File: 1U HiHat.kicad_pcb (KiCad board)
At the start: 2 copper layers, 55.9 x 58.4 mm, 129 parts, among them J1 OH_TRIG, J10 MB, J2 ACCENT, J3 CH_TRIG, J4 OH_OUT, J5 CH_OUT, J6 CB, J7 MB, J8 PWR, J9 CB, P1 2M, P2 A100k, P3 A100k, Q1 BC856, Q10 BC846, Q11 BC846, Q12 BC846, Q13 BC846, Q14 BC846, Q2 BC856, Q3 BC846, Q4 BC846, Q5 BC846, Q6 BC846, Q7 BC846, Q8 BC846, Q9 BC846, U1 TL072, U2 TL072, U3 4584, U4 78L05

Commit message: Complete redesign started
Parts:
- removed REF**: Perforacija, MojaBiblioteka:Perforacija
- C31: value 220n -> 2.2u
- D1, D2: value 1n914 -> 1N914; footprint Diodes_SMD:D_SOD-123F -> Diode_THT:D_DO-35_SOD27_P7.62mm_Horizontal
- J1, J2, J3, J4, J5: footprint 4ms-footprints:PJ301M-12 -> KraakenStuff:PJ301M-12
- J10, J8: footprint MojaBiblioteka:Header 1x3 -> Connector_PinHeader_2.54mm:PinHeader_1x03_P2.54mm_Vertical
- J6: footprint MojaBiblioteka:Header 1x6 -> Connector_PinSocket_2.54mm:PinSocket_1x06_P2.54mm_Vertical
- J7: footprint MojaBiblioteka:Header 1x6 -> Connector_PinHeader_2.54mm:PinHeader_1x06_P2.54mm_Vertical
- J9: footprint MojaBiblioteka:Header 1x3 -> Connector_PinSocket_2.54mm:PinSocket_1x03_P2.54mm_Vertical
- P1, P2, P3: footprint 4ms-footprints:POT-9MM-ALPHA -> KraakenStuff:POT-9MM-ALPHA
- Q1, Q10, Q11, Q12, Q13, Q14, Q2, Q3, Q4, Q5, Q6, Q7, Q8, Q9: footprint MojaBiblioteka:SOT23-BEC -> Package_TO_SOT_SMD:SOT-23
- U1, U2: footprint 4ms-footprints:TSSOP-8_4.4x3mm_Pitch0.65mm -> Package_SO:TSSOP-8_4.4x3mm_P0.65mm
- U3: footprint MusicThingModular:SO14 -> Package_SO:SOIC-14_3.9x8.7mm_P1.27mm
- U4: value 78L05 -> AP7380-50Y-13; footprint MojaBiblioteka:SOT89-In-Gnd-Out -> Package_TO_SOT_SMD:SOT-89-3_Handsoldering
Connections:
- C11 pad 1: +12V -> GND
- C11 pad 2: GND -> -12V
- C28 pad 2: -12V -> +12V
- C32 pad 1: GND -> -12V
- C32 pad 2: +12V -> GND
- C6 pad 1: -12V -> +12V
- Q1 pad 1: Net-(J2-Pad3) -> Net-(Q1-Pad1)
- Q1 pad 2: Net-(Q1-Pad2) -> Net-(J2-PadT)
- Q10 pad 1: GND -> Net-(Q10-Pad1)
- Q10 pad 2: Net-(Q10-Pad2) -> GND
- Q11 pad 1: GND -> Net-(Q11-Pad1)
- Q11 pad 2: Net-(Q11-Pad2) -> GND
- Q12 pad 1: GND -> Net-(Q12-Pad1)
- Q12 pad 2: Net-(Q12-Pad2) -> GND
- Q13 pad 1: Net-(Q13-Pad1) -> Net-(C18-Pad1)
- Q13 pad 2: Net-(C18-Pad1) -> Net-(Q13-Pad2)
- Q14 pad 1: Net-(C24-Pad1) -> Net-(Q14-Pad1)
- Q14 pad 2: Net-(Q14-Pad2) -> Net-(C24-Pad1)
- Q2 pad 1: Net-(J2-Pad3) -> Net-(Q2-Pad1)
- Q2 pad 2: Net-(Q2-Pad2) -> Net-(J2-PadT)
- Q3 pad 1: GND -> Net-(Q3-Pad1)
- Q3 pad 2: Net-(Q3-Pad2) -> GND
- Q4 pad 1: GND -> Net-(Q4-Pad1)
- Q4 pad 2: Net-(Q4-Pad2) -> GND
- Q5 pad 1: Net-(C10-Pad1) -> Net-(C4-Pad2)
- Q5 pad 2: Net-(C4-Pad2) -> Net-(C10-Pad1)
- Q6 pad 1: Net-(Q6-Pad1) -> Net-(C5-Pad1)
- Q6 pad 2: Net-(C5-Pad1) -> Net-(Q6-Pad2)
- Q7 pad 1: Net-(C12-Pad1) -> Net-(Q7-Pad1)
- Q7 pad 2: Net-(Q7-Pad2) -> Net-(C12-Pad1)
- Q9 pad 1: Net-(C22-Pad1) -> Net-(C16-Pad2)
- Q9 pad 2: Net-(C16-Pad2) -> Net-(C22-Pad1)
- R1 pad 2: Net-(Q8-Pad1) -> Net-(Q8-Pad2)
- R10 pad 2: Net-(Q10-Pad2) -> Net-(Q10-Pad1)
- R11 pad 2: Net-(Q7-Pad2) -> Net-(Q7-Pad1)
- R16 pad 1: Net-(Q3-Pad2) -> Net-(Q3-Pad1)
- R18 pad 1: Net-(Q4-Pad2) -> Net-(Q4-Pad1)
- R2 pad 1: Net-(J2-Pad3) -> Net-(J2-PadT)
- R2 pad 2: Net-(Q1-Pad2) -> Net-(Q1-Pad1)
- R22 pad 1: Net-(Q10-Pad2) -> Net-(Q10-Pad1)
- R24 pad 1: Net-(Q6-Pad1) -> Net-(Q6-Pad2)
- R27 pad 1: Net-(Q8-Pad2) -> Net-(Q8-Pad1)
- R28 pad 2: Net-(J5-Pad3) -> Net-(J5-PadT)
- R3 pad 1: Net-(J2-Pad3) -> Net-(J2-PadT)
- R3 pad 2: Net-(Q2-Pad2) -> Net-(Q2-Pad1)
- R30 pad 2: Net-(Q8-Pad1) -> Net-(Q8-Pad2)
- R35 pad 1: Net-(Q11-Pad2) -> Net-(Q11-Pad1)
- R4 pad 2: Net-(J4-Pad3) -> Net-(J4-PadT)
- R43 pad 1: Net-(Q13-Pad1) -> Net-(Q13-Pad2)
- R47 pad 1: Net-(Q14-Pad2) -> Net-(Q14-Pad1)
- R48 pad 2: Net-(Q12-Pad2) -> Net-(Q12-Pad1)
- R5 pad 1: Net-(Q1-Pad2) -> Net-(Q1-Pad1)
- R6 pad 1: Net-(Q2-Pad2) -> Net-(Q2-Pad1)
- R8 pad 1: Net-(J1-Pad3) -> Net-(J1-PadT)
- R8 pad 2: Net-(Q4-Pad2) -> Net-(Q4-Pad1)
- R9 pad 1: Net-(J3-Pad3) -> Net-(J3-PadT)
- R9 pad 2: Net-(Q3-Pad2) -> Net-(Q3-Pad1)
- U4 pad 1: +12V -> GND
- U4 pad 2: GND -> +12V
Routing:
- net +12V: track 140.3 -> 0.00 mm, vias 6 -> 0
- net TO_OH: track 78.2 -> 0.00 mm, vias 2 -> 0
- net -12V: track 70.8 -> 0.00 mm, vias 4 -> 0
- net CH_LVL2: track 68.8 -> 0.00 mm, vias 3 -> 0
- net OH_LVL2: track 65.1 -> 0.00 mm, vias 5 -> 0
- net CH_LVL1: track 50.5 -> 0.00 mm, vias 4 -> 0
- net Net-(C8-Pad2): track 50.3 -> 0.00 mm, vias 4 -> 0
- net Net-(C7-Pad1): track 50.1 -> 0.00 mm, vias 5 -> 0
- net Net-(C30-Pad2): track 48.0 -> 0.00 mm, vias 5 -> 0
- net Net-(C21-Pad1): track 42.7 -> 0.00 mm, vias 3 -> 0
- net OH_LVL1: track 41.7 -> 0.00 mm, vias 2 -> 0
- net Net-(C24-Pad1): track 39.3 -> 0.00 mm, vias 3 -> 0
- net Net-(C12-Pad1): track 38.4 -> 0.00 mm, vias 3 -> 0
- net Net-(J2-Pad3): track 37.6 -> 0.00 mm, vias 2 -> 0
- net Net-(Q10-Pad2): track 34.3 -> 0.00 mm
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
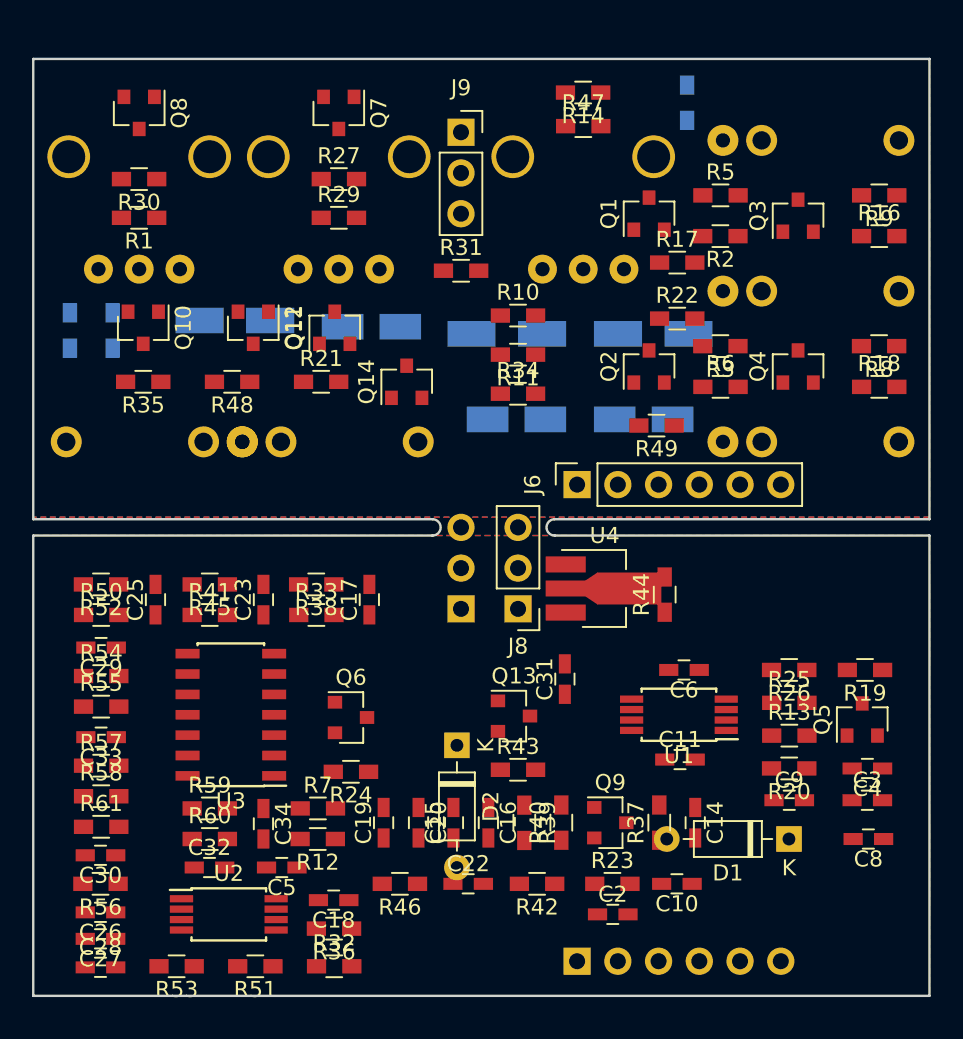
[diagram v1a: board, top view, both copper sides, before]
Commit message: Half of the main board done. Fixed errors in schematics. Added 3D pots
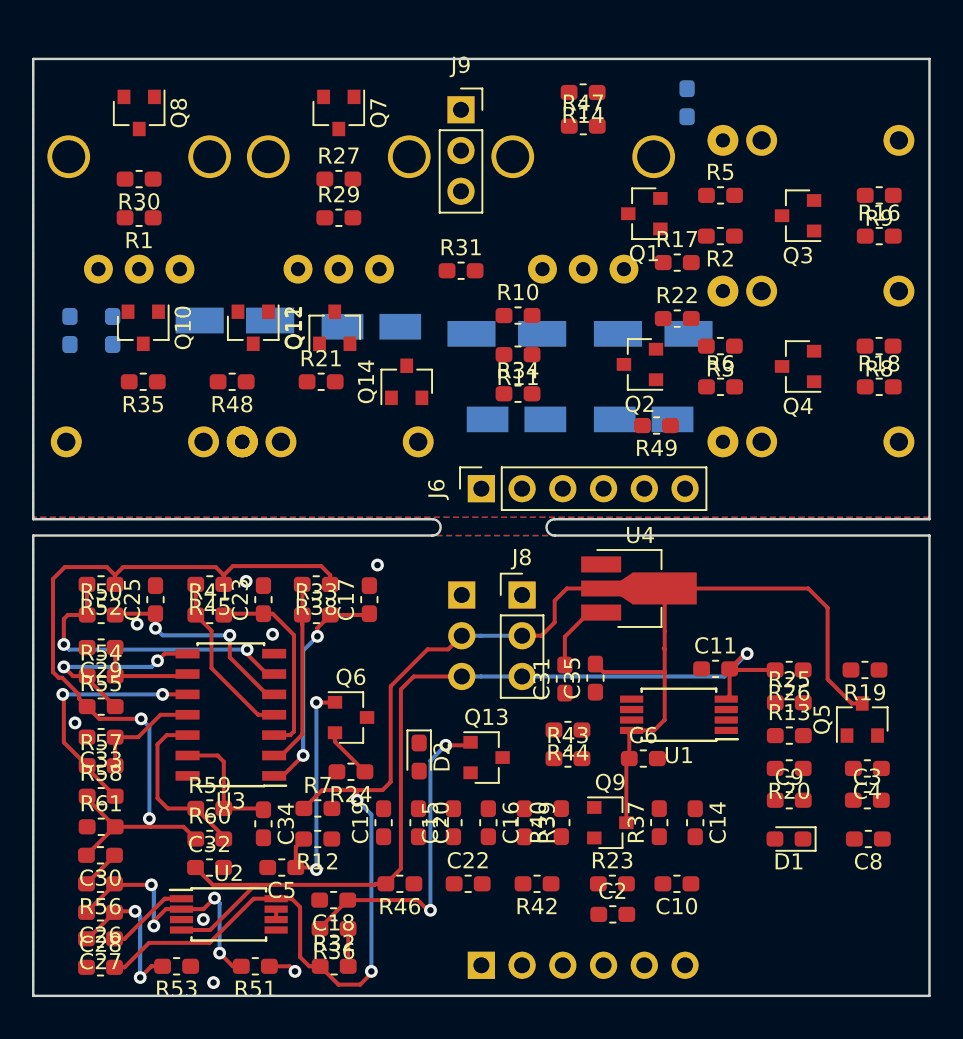
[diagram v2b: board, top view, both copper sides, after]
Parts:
- added C35: 1u, Capacitor_SMD:C_0603_1608Metric_Pad1.05x0.95mm_HandSolder, F.Cu at (124.0, 102.1)
- C1, C13, C7: footprint Capacitors_SMD:CP_Elec_5x5.8 -> Capacitor_SMD:CP_Elec_5x5.8
- C10, C11, C14, C15, C16, C17, C18, C19, C2, C20, C22, C23, C25, C26, C27, C28, C29, C3, C30, C31, C32, C33, C34, C4, C5, C6, C8, C9: footprint Capacitors_SMD:C_0603_HandSoldering -> Capacitor_SMD:C_0603_1608Metric_Pad1.05x0.95mm_HandSolder
- C12, C21, C24: footprint Capacitors_SMD:CP_Elec_4x5.8 -> Capacitor_SMD:CP_Elec_4x5.8
- D1, D2: footprint Diode_THT:D_DO-35_SOD27_P7.62mm_Horizontal -> Diode_SMD:D_0603_1608Metric_Pad1.05x0.95mm_HandSolder
- R1, R10, R11, R12, R13, R14, R15, R16, R17, R18, R19, R2, R20, R21, R22, R23, R24, R25, R26, R27, R28, R29, R3, R30, R31, R32, R33, R34, R35, R36, R37, R38, R39, R4, R40, R41, R42, R43, R44, R45, R46, R47, R48, R49, R5, R50, R51, R52, R53, R54, R55, R56, R57, R58, R59, R6, R60, R61, R7, R8, R9: footprint Resistors_SMD:R_0603_HandSoldering -> Resistor_SMD:R_0603_1608Metric_Pad1.05x0.95mm_HandSolder
- moved R44 10.4 mm to (122.2, 105.3), turned to 180 degrees
- moved C6 6.08 mm to (126.9, 107.1), turned to 0 degrees
- moved C11 6.07 mm to (131.4, 101.5)
- moved J6 5.97 mm to (116.8, 90.3)
- moved J7 5.97 mm to (116.8, 120.0)
- moved R43 3.19 mm to (122.2, 107.1)
- moved Q13 3.10 mm to (117.2, 107.1)
- moved D2 2.47 mm to (113.0, 107.0)
- moved U4 2.21 mm to (126.3, 96.5)
- moved J9 1.40 mm to (115.6, 66.7)
- moved J8 0.90 mm to (119.4, 96.9), turned to 0 degrees
- moved J10 0.87 mm to (115.6, 96.9), turned to 180 degrees
- moved Q2 0.58 mm to (126.7, 82.5), turned to 180 degrees
- moved Q1 0.30 mm to (127.0, 73.1), turned to 180 degrees
- turned Q3 to 180 degrees
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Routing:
- net +12V: track 0.00 -> 101.4 mm, vias 0 -> 2
- net -12V: track 0.00 -> 59.5 mm, vias 0 -> 1
- net Net-(C30-Pad2): track 0.00 -> 51.1 mm, vias 0 -> 2
- net Net-(C18-Pad1): track 0.00 -> 20.2 mm, vias 0 -> 2
- net Net-(R50-Pad1): track 0.00 -> 19.1 mm, vias 0 -> 2
- net Net-(C26-Pad2): track 0.00 -> 17.5 mm, vias 0 -> 4
- net Net-(R57-Pad1): track 0.00 -> 15.5 mm, vias 0 -> 2
- net Net-(C5-Pad1): track 0.00 -> 14.9 mm, vias 0 -> 2
- net Net-(C17-Pad1): track 0.00 -> 14.3 mm, vias 0 -> 2
- net Net-(C25-Pad1): track 0.00 -> 13.4 mm, vias 0 -> 2
- net Net-(R54-Pad1): track 0.00 -> 12.4 mm, vias 0 -> 2
- net Net-(C23-Pad1): track 0.00 -> 12.3 mm
- net Net-(R33-Pad1): track 0.00 -> 11.7 mm
- net Net-(R59-Pad1): track 0.00 -> 10.8 mm
- net Net-(R41-Pad1): track 0.00 -> 10.7 mm
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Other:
- net class Default: clearance 0.2 -> 0.15
- rule trace_clearance: 0.2 -> 0.15

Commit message: Finished main board
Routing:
- net Net-(C8-Pad2): track 0.00 -> 43.0 mm, vias 0 -> 2
- net +5V: track 4.65 -> 40.9 mm, vias 0 -> 2
- net Net-(C10-Pad1): track 0.00 -> 32.6 mm, vias 0 -> 4
- net CH_LVL2: track 0.00 -> 30.4 mm, vias 0 -> 2
- net OH_LVL1: track 0.00 -> 30.0 mm, vias 0 -> 2
- net CH_LVL1: track 0.00 -> 29.5 mm, vias 0 -> 2
- net TO_CH: track 0.00 -> 28.4 mm, vias 0 -> 1
- net OH_LVL2: track 0.00 -> 23.6 mm, vias 0 -> 2
- net Net-(C19-Pad2): track 0.00 -> 20.3 mm, vias 0 -> 2
- net TO_OH: track 0.00 -> 19.5 mm, vias 0 -> 2
- net NOISE: track 6.94 -> 24.5 mm, vias 1 -> 4
- net Net-(C22-Pad1): track 0.00 -> 14.3 mm
- net Net-(C3-Pad2): track 0.00 -> 9.93 mm
- net Net-(C16-Pad2): track 0.00 -> 8.01 mm
- net Net-(Q13-Pad2): track 0.00 -> 5.56 mm
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
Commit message: Finished v0.1
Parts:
- added ~: Perforacija, KraakenStuff:Perforacija, F.Cu at (117.5, 92.6)
- CH Lvl: renamed from P3
- OH Lvl: renamed from P2
- moved R15 0.28 mm to (129.7, 66.5)
- renumbered P1 to Decay
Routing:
- net TO_OH: track 19.5 -> 73.2 mm
- net Net-(C7-Pad1): track 0.00 -> 52.7 mm, vias 0 -> 2
- net CH_LVL2: track 30.4 -> 79.7 mm
- net +12V: track 105.3 -> 153.1 mm
- net OH_LVL2: track 23.6 -> 66.2 mm, vias 2 -> 5
- net Net-(C21-Pad1): track 0.00 -> 41.2 mm, vias 0 -> 1
- net Net-(Q10-Pad1): track 0.00 -> 37.0 mm, vias 0 -> 2
- net Net-(J2-PadT): track 0.00 -> 36.2 mm, vias 0 -> 1
- net Net-(C24-Pad1): track 0.00 -> 32.3 mm, vias 0 -> 1
- net Net-(J4-PadT): track 0.00 -> 30.4 mm
- net Net-(C12-Pad1): track 0.00 -> 29.6 mm, vias 0 -> 2
- net Net-(Q14-Pad1): track 0.00 -> 28.1 mm, vias 0 -> 4
- net Net-(Q7-Pad1): track 0.00 -> 23.4 mm
- net CH_LVL1: track 29.5 -> 51.2 mm
- net Net-(Q11-Pad3): track 0.00 -> 18.9 mm
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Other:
- board text added: "HiHat v0.1"
- board text added: "KraakenStuff"
